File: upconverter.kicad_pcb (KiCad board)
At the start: 2 copper layers, 31 parts, among them J1 Barrel_Jack, J3 SMA_F, J4 USB_B_Mini, J5 SMA_F, U2 SA602A, X1 XO32

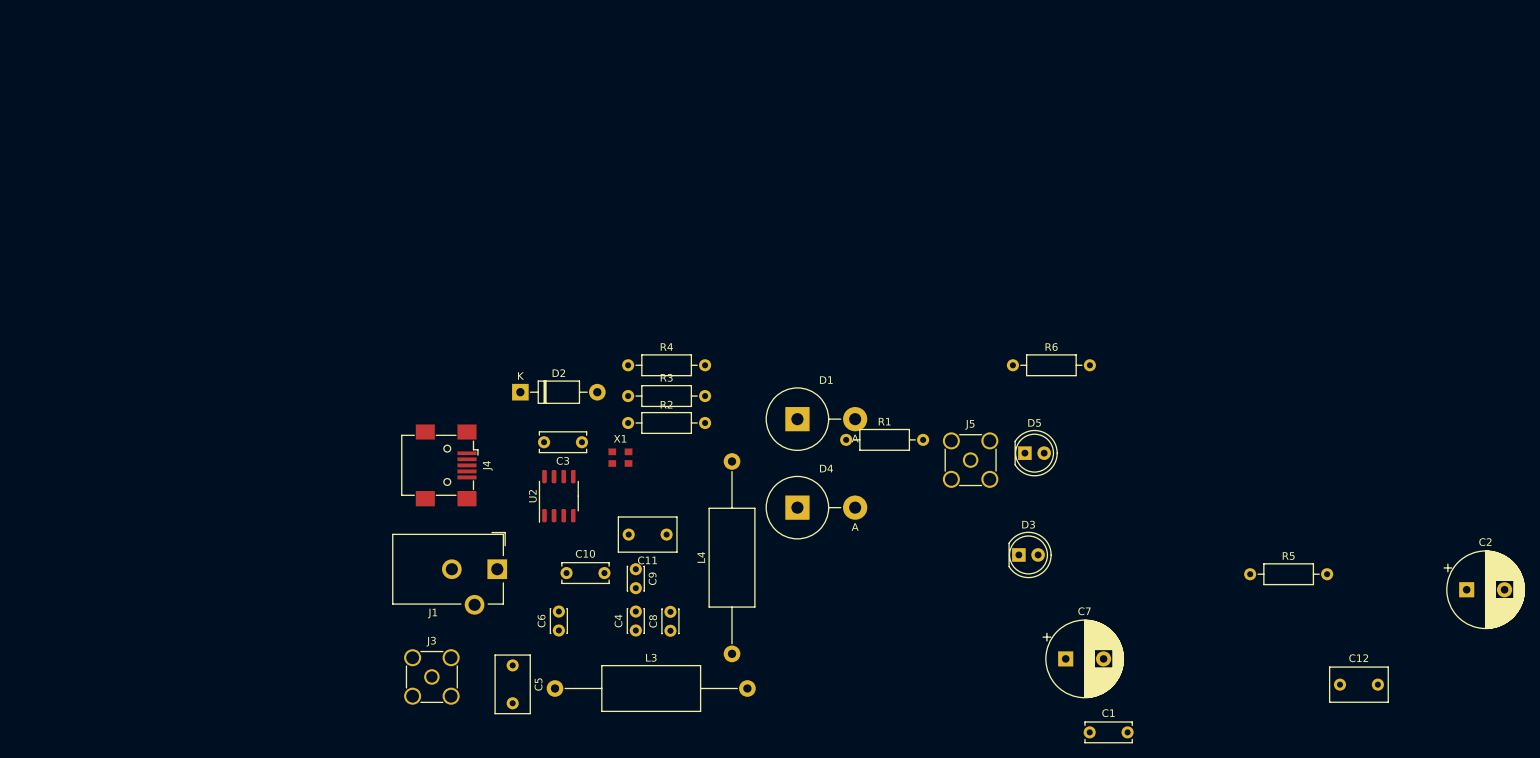
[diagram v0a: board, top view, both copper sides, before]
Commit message: started layout, footprints on new changes
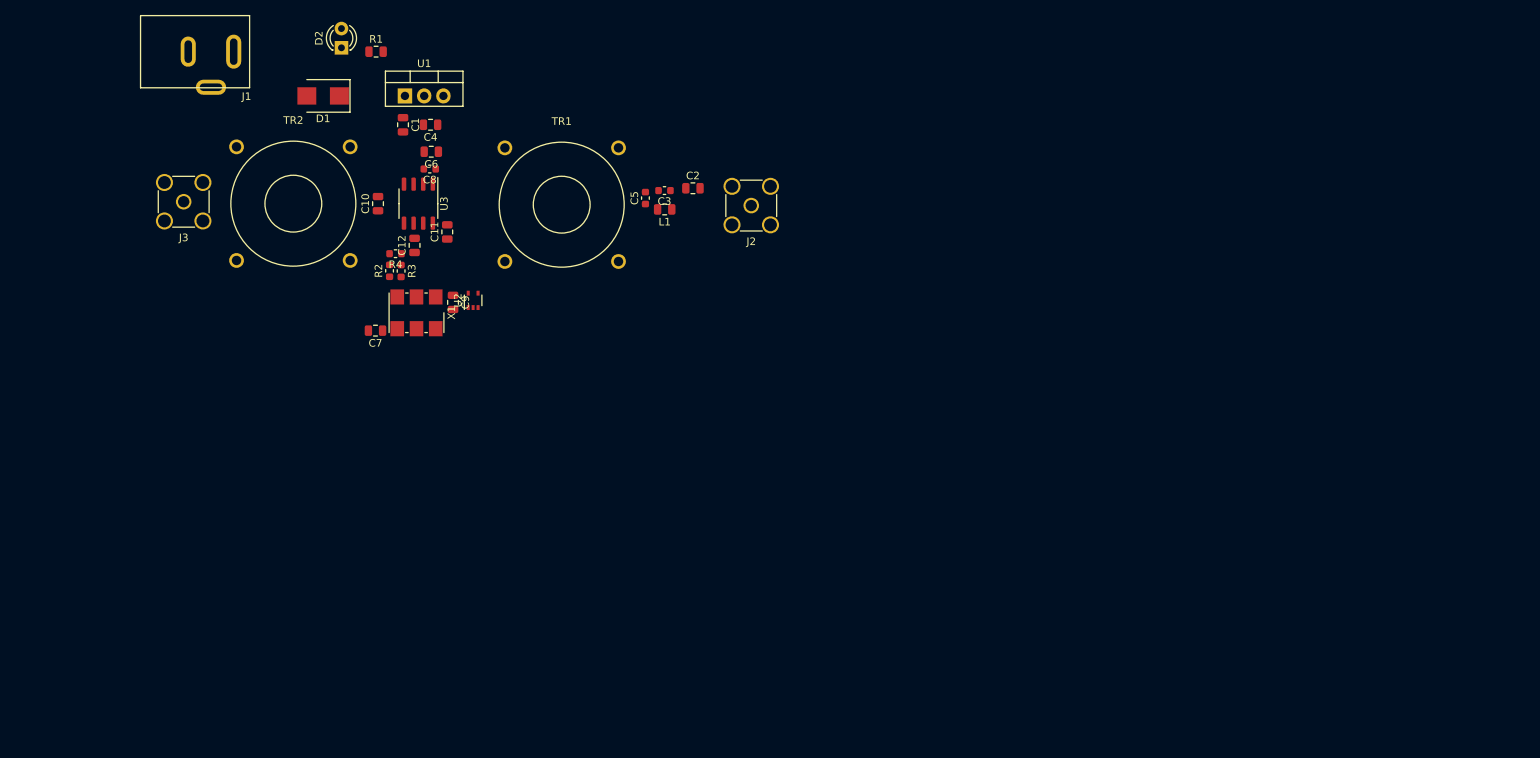
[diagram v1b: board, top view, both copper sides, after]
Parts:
- removed D3: 5v, LED_THT:LED_D5.0mm
- removed D4: 5v, Diode_THT:D_5KPW_P7.62mm_Vertical_AnodeUp
- removed D5: LED, LED_THT:LED_D5.0mm
- removed J4: USB_B_Mini, Connector_USB:USB_Mini-B_Wuerth_65100516121_Horizontal
- removed J5: SMA_F, Connector_Coaxial:SMA_Amphenol_901-144_Vertical
- removed L3, L4: 400nH, Inductor_THT:L_Axial_L12.8mm_D5.8mm_P25.40mm_Horizontal_Fastron_HBCC
- removed R5: 1k, Resistor_THT:R_Axial_DIN0207_L6.3mm_D2.5mm_P10.16mm_Horizontal
- removed R6: 470R, Resistor_THT:R_Axial_DIN0207_L6.3mm_D2.5mm_P10.16mm_Horizontal
- added J2: SMA_F, Connector_Coaxial:SMA_Amphenol_901-144_Vertical, F.Cu at (138.7, 77.0)
- added L1: 400nH, Inductor_SMD:L_0805_2012Metric, F.Cu at (127.3, 77.5)
- added TR1: TRANSF1, ZAM_Custom:fair-rite_2643625002, F.Cu at (113.7, 76.8)
- added TR2: TRANSF1, ZAM_Custom:fair-rite_2643625002, F.Cu at (78.2, 76.7)
- added U1: L7805, Package_TO_SOT_THT:TO-220-3_Vertical, F.Cu at (93.0, 62.5)
- added U3: SA602A, Package_SO:SO-8_3.9x4.9mm_P1.27mm, F.Cu at (94.7, 76.7)
- C1: value 100nF -> 10uF; footprint Capacitor_THT:C_Disc_D6.0mm_W2.5mm_P5.00mm -> Capacitor_SMD:C_0805_2012Metric
- C10: value 100nF -> 220nF; footprint Capacitor_THT:C_Disc_D6.0mm_W2.5mm_P5.00mm -> Capacitor_SMD:C_0805_2012Metric
- C11: value 220nF -> 100nF; footprint Capacitor_THT:C_Disc_D7.5mm_W4.4mm_P5.00mm -> Capacitor_SMD:C_0805_2012Metric
- C12: footprint Capacitor_THT:C_Disc_D7.5mm_W4.4mm_P5.00mm -> Capacitor_SMD:C_0805_2012Metric
- C2: value 220uF -> 220nF; footprint Capacitor_THT:CP_Radial_D10.0mm_P5.00mm -> Capacitor_SMD:C_0805_2012Metric
- C3: value 100nF -> 100pF; footprint Capacitor_THT:C_Disc_D6.0mm_W2.5mm_P5.00mm -> Capacitor_SMD:C_0603_1608Metric
- C4: value 100pF -> 10nF; footprint Capacitor_THT:C_Disc_D3.0mm_W2.0mm_P2.50mm -> Capacitor_SMD:C_0805_2012Metric
- C5: value 220nF -> 100pF; footprint Capacitor_THT:C_Disc_D7.5mm_W4.4mm_P5.00mm -> Capacitor_SMD:C_0603_1608Metric
- C6, C9: value 100pF -> 100nF; footprint Capacitor_THT:C_Disc_D3.0mm_W2.0mm_P2.50mm -> Capacitor_SMD:C_0805_2012Metric
- C7: value 220uF -> 100nF; footprint Capacitor_THT:CP_Radial_D10.0mm_P5.00mm -> Capacitor_SMD:C_0805_2012Metric
- C8: footprint Capacitor_THT:C_Disc_D3.0mm_W2.0mm_P2.50mm -> Capacitor_SMD:C_0603_1608Metric
- D1: value 3.3v -> SK24; footprint Diode_THT:D_5KPW_P7.62mm_Vertical_AnodeUp -> Diode_SMD:D_SMB
- D2: value 1N4007 -> 5v; footprint Diode_THT:D_DO-41_SOD81_P10.16mm_Horizontal -> LED_THT:LED_D3.0mm
- J1: footprint Connector_BarrelJack:BarrelJack_CUI_PJ-102AH_Horizontal -> ZAM_Custom:PJ-002A_2.1_5.5_Barrel_Jack_CUI
- R1: footprint Resistor_THT:R_Axial_DIN0207_L6.3mm_D2.5mm_P10.16mm_Horizontal -> Resistor_SMD:R_0805_2012Metric
- R2, R3, R4: footprint Resistor_THT:R_Axial_DIN0207_L6.3mm_D2.5mm_P10.16mm_Horizontal -> Resistor_SMD:R_0603_1608Metric
- U2: value SA602A -> TPS71533__SC70; footprint Package_SO:SO-8_3.9x4.9mm_P1.27mm -> Package_TO_SOT_SMD:SOT-353_SC-70-5
- X1: footprint Oscillator:Oscillator_SMD_EuroQuartz_XO32-4Pin_3.2x2.5mm -> Oscillator:Oscillator_SMD_IDT_JU6-6_7.0x5.0mm_P2.54mm
- moved C12 135.2 mm to (94.2, 82.2), turned to 90 degrees
- moved C1 121.0 mm to (92.7, 66.3), turned to 270 degrees
- moved C2 115.1 mm to (131.0, 74.7)
- moved C7 100.9 mm to (89.1, 93.5), turned to 180 degrees
- moved R1 80.5 mm to (89.2, 56.6)
- moved J1 76.7 mm to (70.4, 56.6), turned to 0 degrees
- moved D1 75.8 mm to (82.2, 62.5), turned to 180 degrees
- moved C4 72.1 mm to (96.3, 66.3), turned to 180 degrees
- moved J3 70.8 mm to (63.8, 76.5), turned to 180 degrees
- moved C8 68.7 mm to (96.2, 72.1), turned to 180 degrees
- moved C6 65.4 mm to (96.4, 69.8), turned to 180 degrees
- moved C5 64.1 mm to (124.7, 76.0), turned to 90 degrees
- moved C10 54.8 mm to (89.4, 76.7), turned to 90 degrees
- moved D2 51.2 mm to (84.6, 56.1), turned to 90 degrees
- moved C11 49.3 mm to (98.6, 80.4), turned to 90 degrees
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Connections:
- C1 pad 1: +3V3 -> Net-(C1-Pad1)
- C10 pad 2: GND -> Net-(C10-Pad2)
- C11 pad 1: Net-(C11-Pad1) -> GND
- C11 pad 2: Net-(C11-Pad2) -> +5V
- C2 pad 1: +3V3 -> Net-(C2-Pad1)
- C2 pad 2: GND -> Net-(C2-Pad2)
- C3 pad 1: GND -> Net-(C2-Pad1)
- C3 pad 2: +5V -> Net-(C3-Pad2)
- C4 pad 1: Net-(C4-Pad1) -> +5V
- C5 pad 2: Net-(C5-Pad2) -> Net-(C3-Pad2)
- C6 pad 1: Net-(C5-Pad1) -> +5V
- C7 pad 1: +5V -> +3V3
- C8 pad 1: Net-(C4-Pad1) -> Net-(C8-Pad1)
- C8 pad 2: GND -> Net-(C8-Pad2)
- C9 pad 1: Net-(C9-Pad1) -> +3V3
- D1 pad 1: +3V3 -> Net-(C1-Pad1)
- D1 pad 2: GND -> Net-(D1-Pad2)
- D2 pad 1: +5V -> Net-(D2-Pad1)
- D2 pad 2: Net-(D2-Pad2) -> +5V
- J1 pad 1: Net-(D2-Pad2) -> Net-(D1-Pad2)
- J3 pad 1: Net-(C5-Pad2) -> Net-(J3-Pad1)
- J3 pad 2: GND -> Net-(J3-Pad2)
- R1 pad 1: Net-(D3-Pad1) -> Net-(D2-Pad1)
- U2 pad 1: Net-(C9-Pad1) -> Net-(U2-Pad1)
- U2 pad 2: Net-(C10-Pad1) -> GND
- U2 pad 3: GND -> Net-(U2-Pad3)
- U2 pad 4: Net-(C11-Pad2) -> +5V
- U2 pad 5: Net-(U2-Pad5) -> +3V3

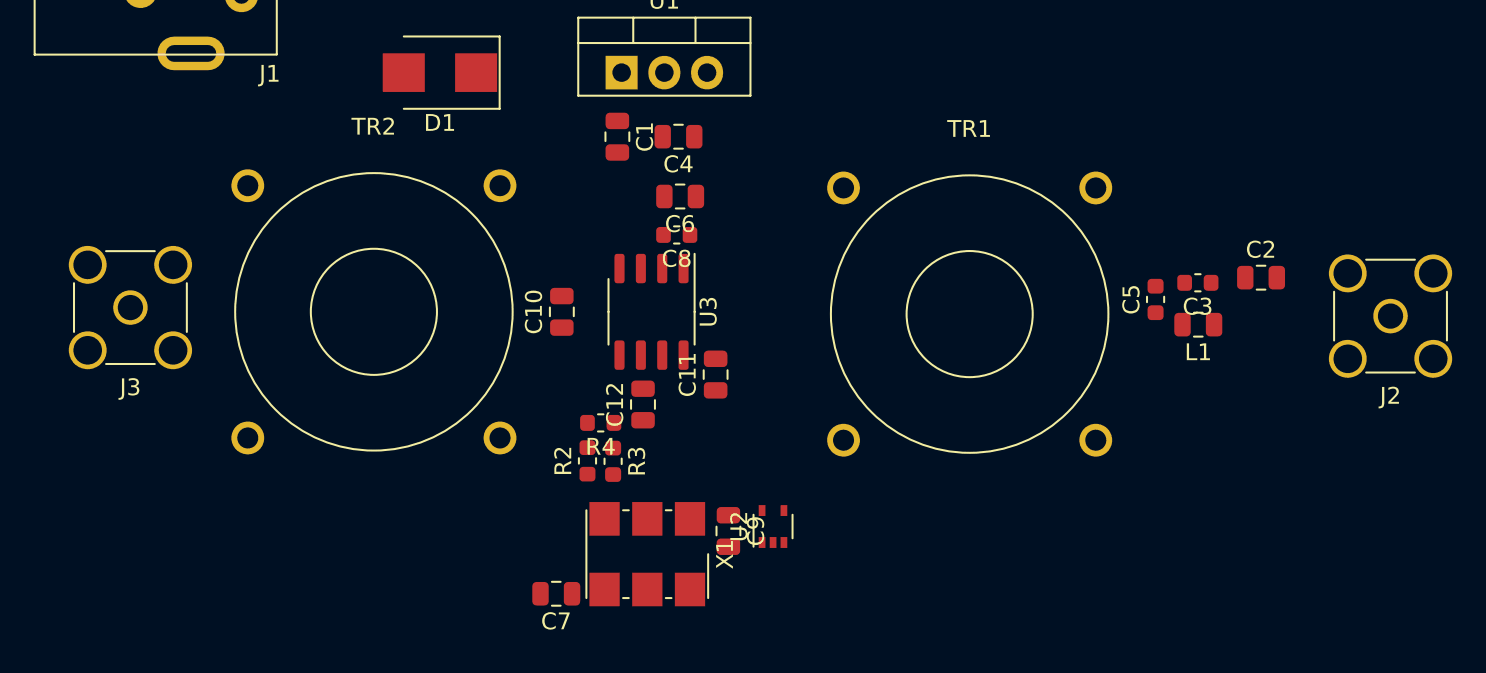
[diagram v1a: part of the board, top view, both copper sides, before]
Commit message: input LPF
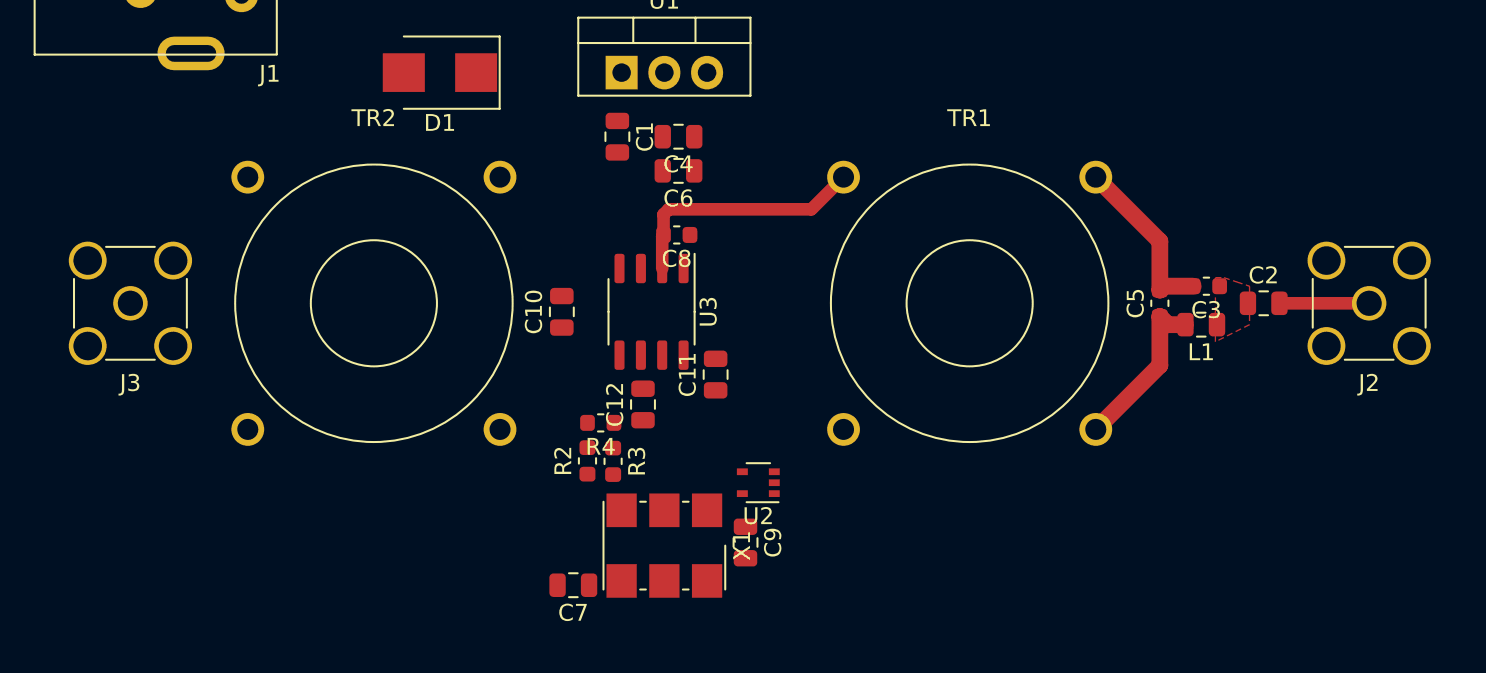
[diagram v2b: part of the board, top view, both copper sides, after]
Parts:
- moved U2 2.75 mm to (101.1, 86.9), turned to 180 degrees
- moved C2 1.53 mm to (131.1, 76.2)
- moved C6 1.53 mm to (96.3, 68.3)
- moved J2 1.48 mm to (137.4, 76.2)
- moved C9 1.22 mm to (100.3, 90.4)
- moved X1 1.14 mm to (95.5, 90.6)
- moved C7 1.14 mm to (90.1, 93.0)
- moved TR1 0.64 mm to (113.7, 76.2)
- moved C3 0.55 mm to (127.7, 75.2)
- moved TR2 0.51 mm to (78.2, 76.2)
- moved C5 0.34 mm to (125.0, 76.2)
- moved J3 0.25 mm to (63.8, 76.2)
- moved L1 0.18 mm to (127.4, 77.5)
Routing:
- net Net-(C8-Pad2): track 0.00 -> 14.9 mm
- net Net-(C3-Pad2): track 0.00 -> 10.4 mm
- net Net-(C5-Pad1): track 0.00 -> 10.0 mm
- net Net-(C2-Pad2): track 0.00 -> 5.33 mm
- added copper zone on F.Cu, net Net-(C2-Pad1)

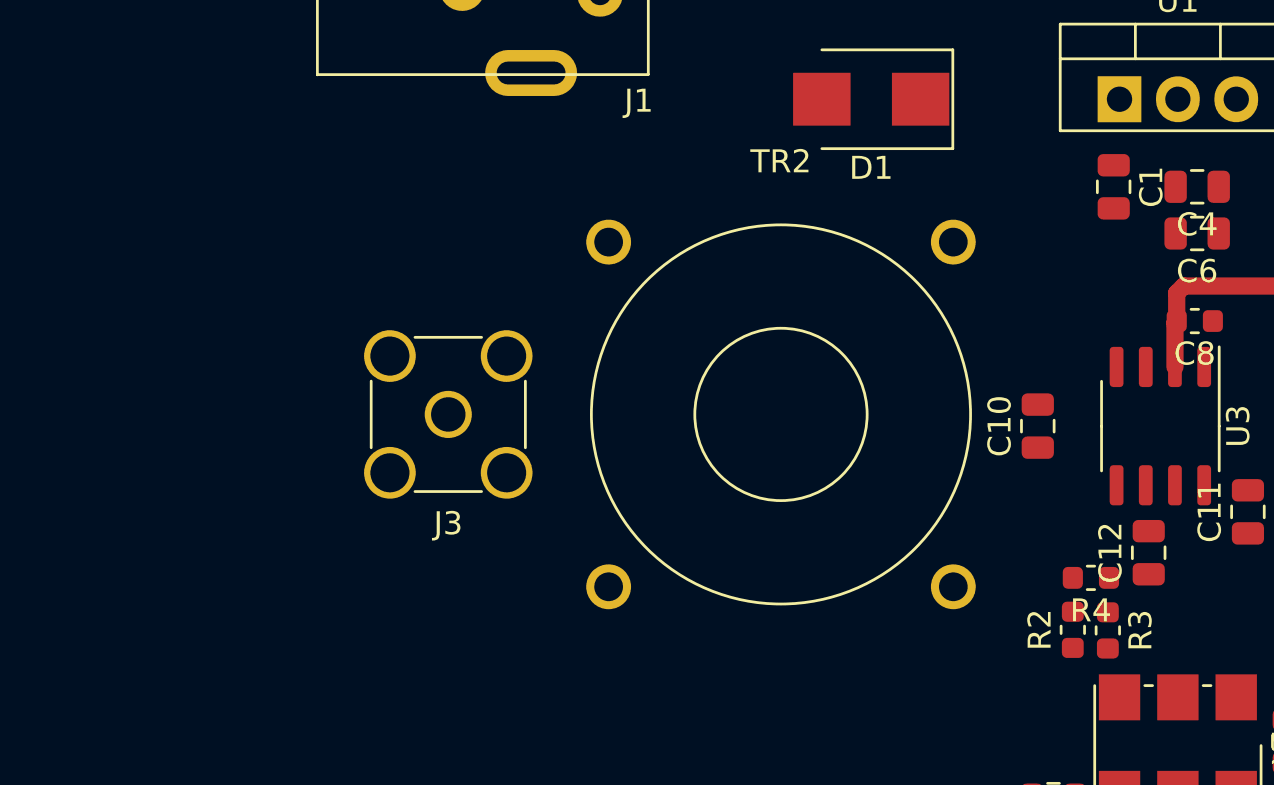
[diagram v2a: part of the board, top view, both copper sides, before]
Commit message: Updated output filter
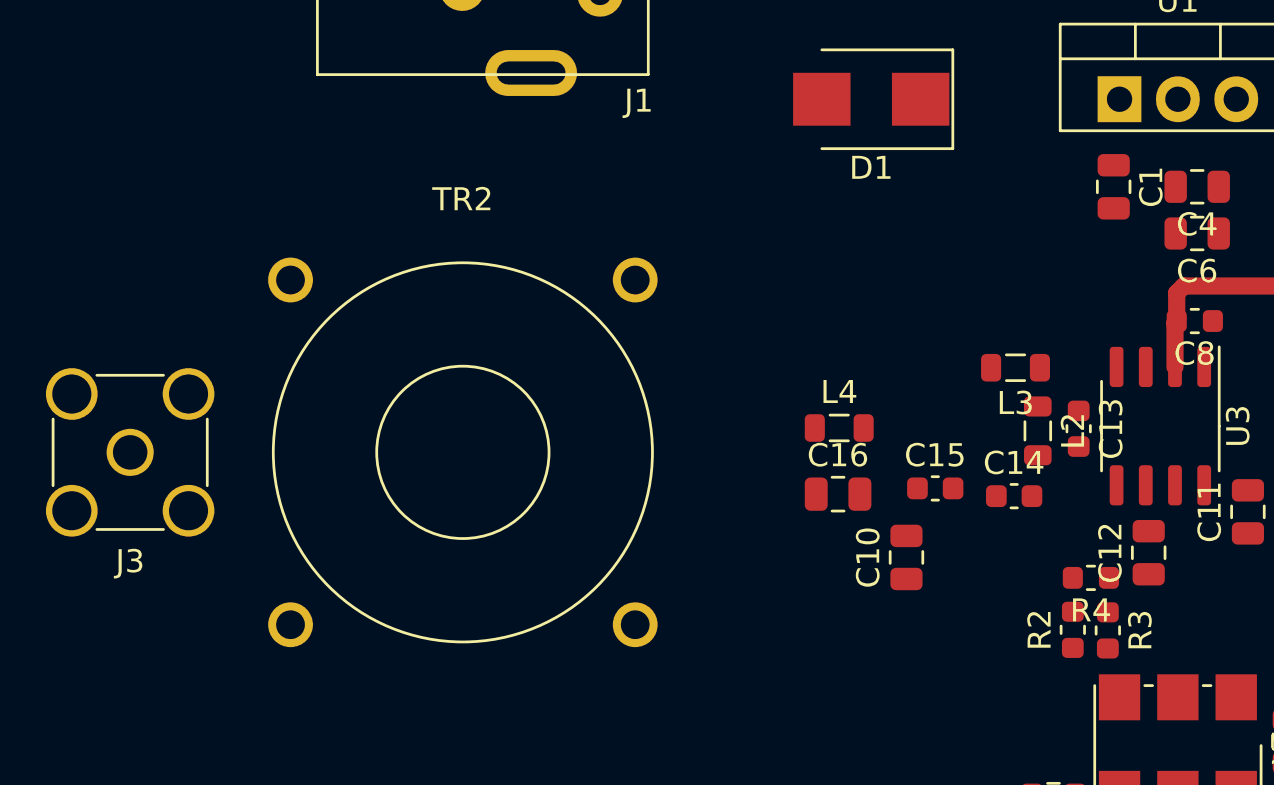
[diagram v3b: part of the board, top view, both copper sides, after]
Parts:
- added C13: 18pF, Capacitor_SMD:C_0603_1608Metric, F.Cu at (91.2, 76.8)
- added C14: 18pF, Capacitor_SMD:C_0603_1608Metric, F.Cu at (88.4, 79.8)
- added C15: OMIT4.3pF, Capacitor_SMD:C_0603_1608Metric, F.Cu at (84.9, 79.4)
- added C16: 18pF, Capacitor_SMD:C_0805_2012Metric, F.Cu at (80.7, 79.7)
- added L2: 33nH, Inductor_SMD:L_0805_2012Metric, F.Cu at (89.4, 76.9)
- added L3: 33nH, Inductor_SMD:L_0805_2012Metric, F.Cu at (88.4, 74.2)
- added L4: 33nH, Inductor_SMD:L_0805_2012Metric, F.Cu at (80.8, 76.8)
- C10: value 220nF -> 18pF
- moved TR2 13.9 mm to (64.4, 77.9)
- moved J3 13.9 mm to (49.9, 77.9)
- moved C10 8.08 mm to (83.7, 82.4)
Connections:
- TR2 pad 1: Net-(C10-Pad1) -> Net-(C10-Pad2)
- U3 pad 4: Net-(C10-Pad2) -> Net-(C13-Pad1)
- U3 pad 5: Net-(C10-Pad1) -> Net-(C13-Pad2)
